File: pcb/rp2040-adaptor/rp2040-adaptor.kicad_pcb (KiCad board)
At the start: 2 copper layers, 35 x 29 mm, 3 parts, among them J1 Conn_01x09, J2 Conn_01x09

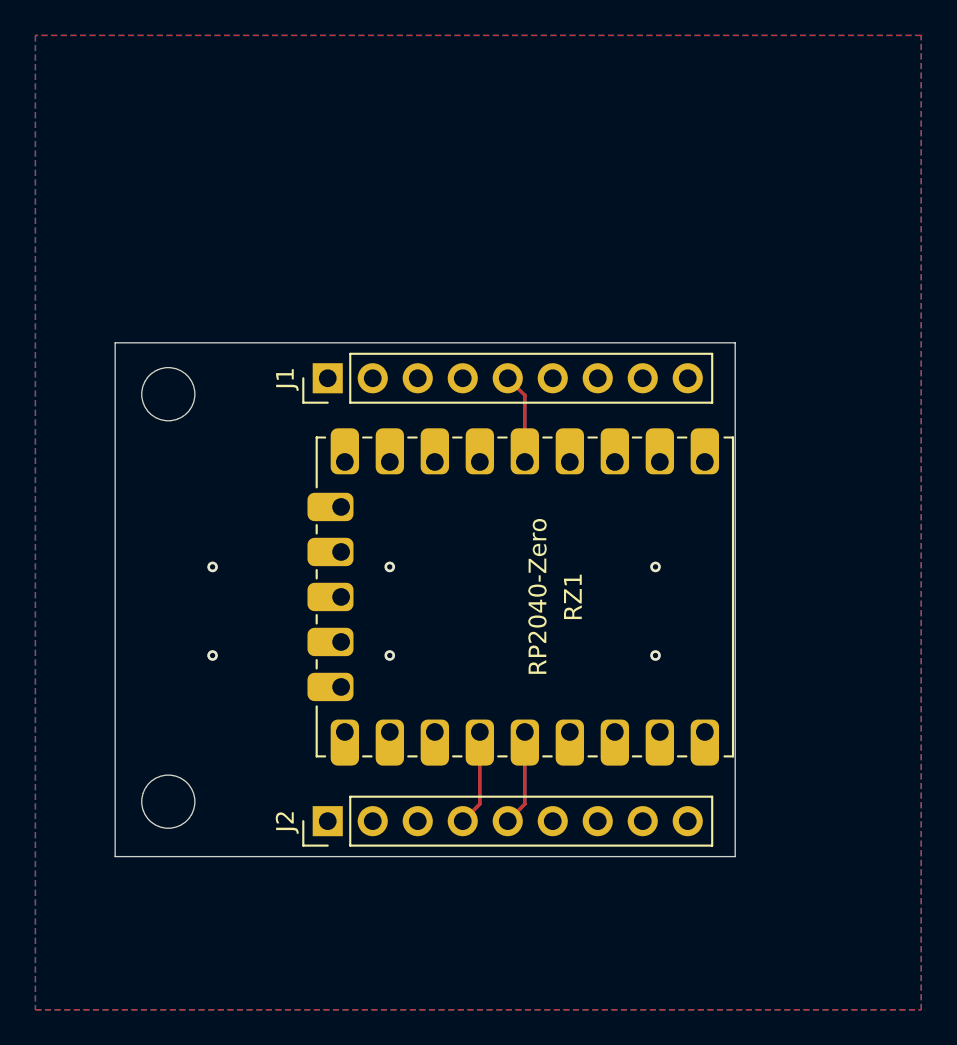
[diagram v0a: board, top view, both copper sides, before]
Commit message: make room for bottom surface
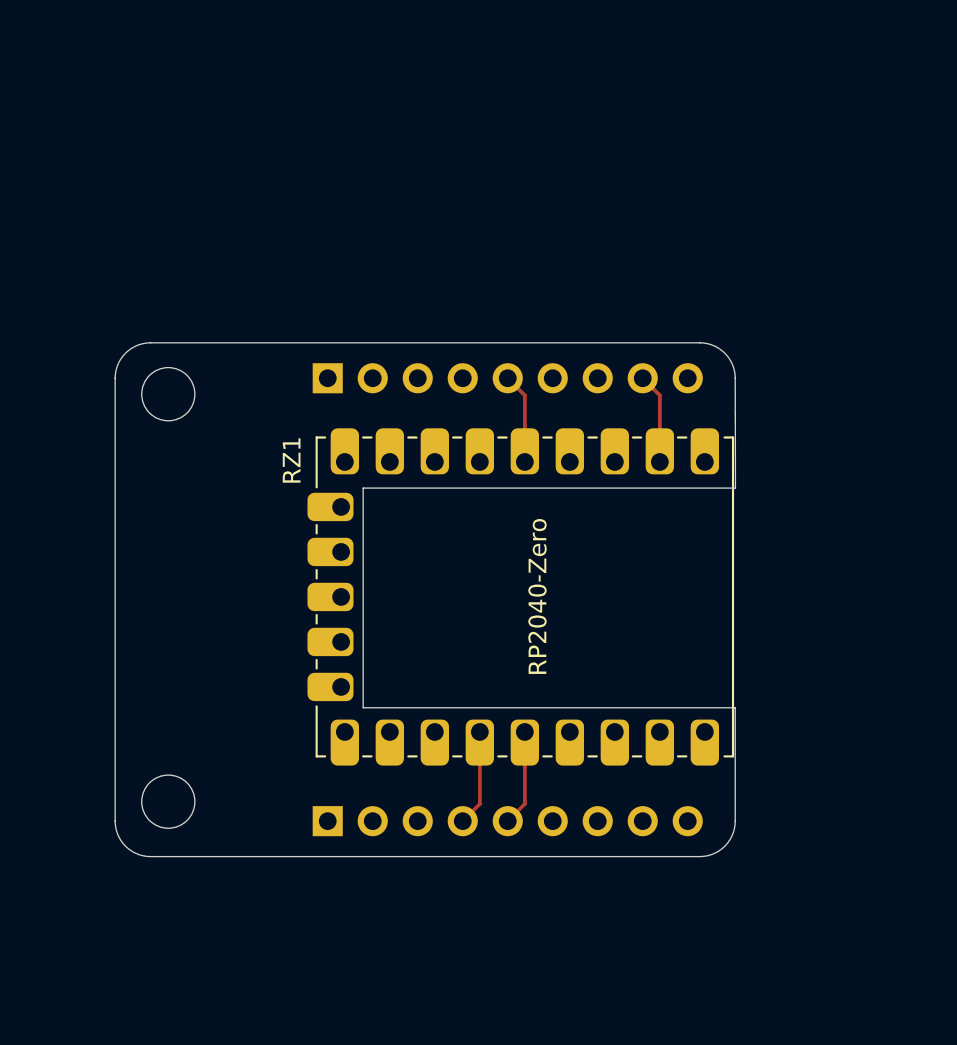
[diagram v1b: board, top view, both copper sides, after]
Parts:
- J1, J2: moved to B.Cu
- turned J1 to -90 degrees
- turned J2 to -90 degrees
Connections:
- RZ1 pad 10: unconnected-(RZ1-GP9-Pad10) -> (no net)
- RZ1 pad 11: unconnected-(RZ1-GP10-Pad11) -> (no net)
- RZ1 pad 12: unconnected-(RZ1-GP11-Pad12) -> (no net)
- RZ1 pad 13: unconnected-(RZ1-GP12-Pad13) -> (no net)
- RZ1 pad 14: unconnected-(RZ1-GP13-Pad14) -> (no net)
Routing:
- net GND: track 0.00 -> 5.12 mm, vias 6 -> 0
- removed copper zone on B.Cu, net GND
- removed copper zone on F.Cu, net GND
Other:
- outline, holes or cut-outs redrawn

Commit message: update docs
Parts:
- J1, J2: footprint Connector_PinHeader_2.54mm:PinHeader_1x09_P2.54mm_Vertical -> Connector_PinSocket_2.54mm:PinSocket_1x09_P2.54mm_Vertical
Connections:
- RZ1 pad 10: (no net) -> unconnected-(RZ1-GP9-Pad10)
- RZ1 pad 11: (no net) -> unconnected-(RZ1-GP10-Pad11)
- RZ1 pad 12: (no net) -> unconnected-(RZ1-GP11-Pad12)
- RZ1 pad 13: (no net) -> unconnected-(RZ1-GP12-Pad13)
- RZ1 pad 14: (no net) -> unconnected-(RZ1-GP13-Pad14)
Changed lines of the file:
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@@
 		(sheetname "/")
 		(sheetfile "rp2040-adaptor.kicad_sch")
+		(units
+			(unit
+				(name "A")
+				(pins "1" "2" "3" "4" "5" "6" "7" "8" "9" "10" "23" "22" "21" "20" "19"
+					"18" "17" "16" "15" "14" "13" "12" "11"
+				)
+			)
+		)
 		(attr through_hole)
 		(duplicate_pad_numbers_are_jumpers no)
@@
 			(remove_unused_layers no)
 			(roundrect_rratio 0.25)
+			(net "unconnected-(RZ1-GP9-Pad10)")
+			(pinfunction "GP9_10")
+			(pintype "bidirectional")
 			(thermal_bridge_angle 45)
 			(padstack
@@
 			(remove_unused_layers no)
 			(roundrect_rratio 0.25)
+			(net "unconnected-(RZ1-GP10-Pad11)")
+			(pinfunction "GP10_11")
+			(pintype "bidirectional")
 			(thermal_bridge_angle 45)
 			(padstack
@@
 			(remove_unused_layers no)
 			(roundrect_rratio 0.25)
+			(net "unconnected-(RZ1-GP11-Pad12)")
+			(pinfunction "GP11_12")
+			(pintype "bidirectional")
 			(thermal_bridge_angle 45)
 			(padstack
@@
 			(remove_unused_layers no)
 			(roundrect_rratio 0.25)
+			(net "unconnected-(RZ1-GP12-Pad13)")
+			(pinfunction "GP12_13")
+			(pintype "bidirectional")
 			(thermal_bridge_angle 45)
 			(padstack
@@
 			(remove_unused_layers no)
 			(roundrect_rratio 0.25)
+			(net "unconnected-(RZ1-GP13-Pad14)")
+			(pinfunction "GP13_14")
+			(pintype "bidirectional")
 			(thermal_bridge_angle 45)
 			(padstack
@@
 		)
 	)
-	(footprint "Connector_PinHeader_2.54mm:PinHeader_1x09_P2.54mm_Vertical"
+	(footprint "Connector_PinSocket_2.54mm:PinSocket_1x09_P2.54mm_Vertical"
 		(layer "B.Cu")
 		(at 106.5 99.35 -90)
-		(descr "Through hole straight pin header, 1x09, 2.54mm pitch, single row")
-		(tags "Through hole pin header THT 1x09 2.54mm single row")
+		(descr "Through hole straight socket strip, 1x09, 2.54mm pitch, single row (from Kicad 4.0.7), script generated")
+		(tags "Through hole socket strip THT 1x09 2.54mm single row")
 		(property "Reference" "J2"
-			(at 0 2.38 90)
+			(at 0 2.77 90)
 			(layer "B.SilkS")
 			(effects
@@
 		)
 		(property "Value" "Conn_01x09"
-			(at 0 -22.7 90)
+			(at 0 -23.09 90)
 			(layer "B.Fab")
 			(effects
@@
 		(sheetname "/")
 		(sheetfile "rp2040-adaptor.kicad_sch")
+		(units
+			(unit
+				(name "A")
+				(pins "1" "2" "3" "4" "5" "6" "7" "8" "9")
+			)
+		)
 		(attr through_hole)
 		(duplicate_pad_numbers_are_jumpers no)
 		(fp_line
-			(start -1.38 1.38)
-			(end 0 1.38)
+			(start 0 1.33)
+			(end 1.33 1.33)
 			(stroke
 				(width 0.12)
@@
 		)
 		(fp_line
-			(start -1.38 0)
-			(end -1.38 1.38)
+			(start 1.33 1.33)
+			(end 1.33 0)
 			(stroke
 				(width 0.12)
@@
 		)
 		(fp_line
-			(start -1.38 -1.27)
-			(end 1.38 -1.27)
+			(start -1.33 -1.27)
+			(end 1.33 -1.27)
 			(stroke
 				(width 0.12)
@@
 		)
 		(fp_line
-			(start -1.38 -1.27)
-			(end -1.38 -21.7)
+			(start -1.33 -1.27)
+			(end -1.33 -21.65)
 			(stroke
 				(width 0.12)
@@
 		)
 		(fp_line
-			(start 1.38 -1.27)
-			(end 1.38 -21.7)
+			(start 1.33 -1.27)
+			(end 1.33 -21.65)
 			(stroke
 				(width 0.12)
@@
 		)
 		(fp_line
-			(start -1.38 -21.7)
-			(end 1.38 -21.7)
+			(start -1.33 -21.65)
+			(end 1.33 -21.65)
 			(stroke
 				(width 0.12)
@@
 			(layer "B.SilkS")
 		)
-		(fp_rect
+		(fp_line
 			(start -1.77 1.77)
+			(end 1.77 1.77)
+			(stroke
+				(width 0.05)
+				(type solid)
+			)
+			(layer "B.CrtYd")
+		)
+		(fp_line
+			(start 1.77 1.77)
 			(end 1.77 -22.09)
 			(stroke
@@
 				(type solid)
 			)
-			(fill no)
 			(layer "B.CrtYd")
 		)
 		(fp_line
-			(start -0.635 1.27)
-			(end 1.27 1.27)
+			(start -1.77 -22.09)
+			(end -1.77 1.77)
+			(stroke
+				(width 0.05)
+				(type solid)
+			)
+			(layer "B.CrtYd")
+		)
+		(fp_line
+			(start 1.77 -22.09)
+			(end -1.77 -22.09)
+			(stroke
+				(width 0.05)
+				(type solid)
+			)
+			(layer "B.CrtYd")
+		)
+		(fp_line
+			(start -1.27 1.27)
+			(end 0.635 1.27)
 			(stroke
 				(width 0.1)
@@
 		)
 		(fp_line
-			(start 1.27 1.27)
+			(start 0.635 1.27)
+			(end 1.27 0.635)
+			(stroke
+				(width 0.1)
+				(type solid)
+			)
+			(layer "B.Fab")
+		)
+		(fp_line
+			(start 1.27 0.635)
 			(end 1.27 -21.59)
 			(stroke
@@
 		)
 		(fp_line
-			(start -1.27 0.635)
-			(end -0.635 1.27)
-			(stroke
-				(width 0.1)
-				(type solid)
-			)
-			(layer "B.Fab")
-		)
-		(fp_line
 			(start -1.27 -21.59)
-			(end -1.27 0.635)
+			(end -1.27 1.27)
 			(stroke
 				(width 0.1)
@@
 		)
 		(fp_text user "${REFERENCE}"
-			(at 0 -10.16 0)
+			(at 0 -10.16 180)
 			(layer "B.Fab")
 			(effects
@@
 		)
 		(embedded_fonts no)
-		(model "${KICAD10_3DMODEL_DIR}/Connector_PinHeader_2.54mm.3dshapes/PinHeader_1x09_P2.54mm_Vertical.step"
+		(model "${KICAD10_3DMODEL_DIR}/Connector_PinSocket_2.54mm.3dshapes/PinSocket_1x09_P2.54mm_Vertical.step"
 			(offset
 				(xyz 0 0 0)
@@
 		)
 	)
-	(footprint "Connector_PinHeader_2.54mm:PinHeader_1x09_P2.54mm_Vertical"
+	(footprint "Connector_PinSocket_2.54mm:PinSocket_1x09_P2.54mm_Vertical"
 		(layer "B.Cu")
 		(at 106.5 74.35 -90)
-		(descr "Through hole straight pin header, 1x09, 2.54mm pitch, single row")
-		(tags "Through hole pin header THT 1x09 2.54mm single row")
+		(descr "Through hole straight socket strip, 1x09, 2.54mm pitch, single row (from Kicad 4.0.7), script generated")
+		(tags "Through hole socket strip THT 1x09 2.54mm single row")
 		(property "Reference" "J1"
-			(at 0 2.38 90)
+			(at 0 2.77 90)
 			(layer "B.SilkS")
 			(effects
@@
 		)
 		(property "Value" "Conn_01x09"
-			(at 0 -22.7 90)
+			(at 0 -23.09 90)
 			(layer "B.Fab")
 			(effects
@@
 		(sheetname "/")
 		(sheetfile "rp2040-adaptor.kicad_sch")
+		(units
+			(unit
+				(name "A")
+				(pins "1" "2" "3" "4" "5" "6" "7" "8" "9")
+			)
+		)
 		(attr through_hole)
 		(duplicate_pad_numbers_are_jumpers no)
 		(fp_line
-			(start -1.38 1.38)
-			(end 0 1.38)
+			(start 0 1.33)
+			(end 1.33 1.33)
 			(stroke
 				(width 0.12)
@@
 		)
 		(fp_line
-			(start -1.38 0)
-			(end -1.38 1.38)
+			(start 1.33 1.33)
+			(end 1.33 0)
 			(stroke
 				(width 0.12)
@@
 		)
 		(fp_line
-			(start -1.38 -1.27)
-			(end 1.38 -1.27)
+			(start -1.33 -1.27)
+			(end 1.33 -1.27)
 			(stroke
 				(width 0.12)
@@
 		)
 		(fp_line
-			(start -1.38 -1.27)
-			(end -1.38 -21.7)
+			(start -1.33 -1.27)
+			(end -1.33 -21.65)
 			(stroke
 				(width 0.12)
@@
 		)
 		(fp_line
-			(start 1.38 -1.27)
-			(end 1.38 -21.7)
+			(start 1.33 -1.27)
+			(end 1.33 -21.65)
 			(stroke
 				(width 0.12)
@@
 		)
 		(fp_line
-			(start -1.38 -21.7)
-			(end 1.38 -21.7)
+			(start -1.33 -21.65)
+			(end 1.33 -21.65)
 			(stroke
 				(width 0.12)
@@
 			(layer "B.SilkS")
 		)
-		(fp_rect
+		(fp_line
 			(start -1.77 1.77)
+			(end 1.77 1.77)
+			(stroke
+				(width 0.05)
+				(type solid)
+			)
+			(layer "B.CrtYd")
+		)
+		(fp_line
+			(start 1.77 1.77)
 			(end 1.77 -22.09)
 			(stroke
@@
 				(type solid)
 			)
-			(fill no)
 			(layer "B.CrtYd")
 		)
 		(fp_line
-			(start -0.635 1.27)
-			(end 1.27 1.27)
+			(start -1.77 -22.09)
+			(end -1.77 1.77)
+			(stroke
+				(width 0.05)
+				(type solid)
+			)
+			(layer "B.CrtYd")
+		)
+		(fp_line
+			(start 1.77 -22.09)
+			(end -1.77 -22.09)
+			(stroke
+				(width 0.05)
+				(type solid)
+			)
+			(layer "B.CrtYd")
+		)
+		(fp_line
+			(start -1.27 1.27)
+			(end 0.635 1.27)
 			(stroke
 				(width 0.1)
@@
 		)
 		(fp_line
-			(start 1.27 1.27)
+			(start 0.635 1.27)
+			(end 1.27 0.635)
+			(stroke
+				(width 0.1)
+				(type solid)
+			)
+			(layer "B.Fab")
+		)
+		(fp_line
+			(start 1.27 0.635)
 			(end 1.27 -21.59)
 			(stroke
@@
 		)
 		(fp_line
-			(start -1.27 0.635)
-			(end -0.635 1.27)
-			(stroke
-				(width 0.1)
-				(type solid)
-			)
-			(layer "B.Fab")
-		)
-		(fp_line
 			(start -1.27 -21.59)
-			(end -1.27 0.635)
+			(end -1.27 1.27)
 			(stroke
 				(width 0.1)
@@
 		)
 		(fp_text user "${REFERENCE}"
-			(at 0 -10.16 0)
+			(at 0 -10.16 180)
 			(layer "B.Fab")
 			(effects
@@
 		)
 		(embedded_fonts no)
-		(model "${KICAD10_3DMODEL_DIR}/Connector_PinHeader_2.54mm.3dshapes/PinHeader_1x09_P2.54mm_Vertical.step"
+		(model "${KICAD10_3DMODEL_DIR}/Connector_PinSocket_2.54mm.3dshapes/PinSocket_1x09_P2.54mm_Vertical.step"
 			(offset
 				(xyz 0 0 0)
